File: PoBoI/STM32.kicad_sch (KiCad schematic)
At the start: 24 parts, among them U17 LP5907SNX-3.3, U21 74AC14MTCX, U22 LTC4304CMS#PBF, U26 ISL3259EIRZ, U6 STM32F103RET6, Y1 ABS07-166-32.768KHZ-T

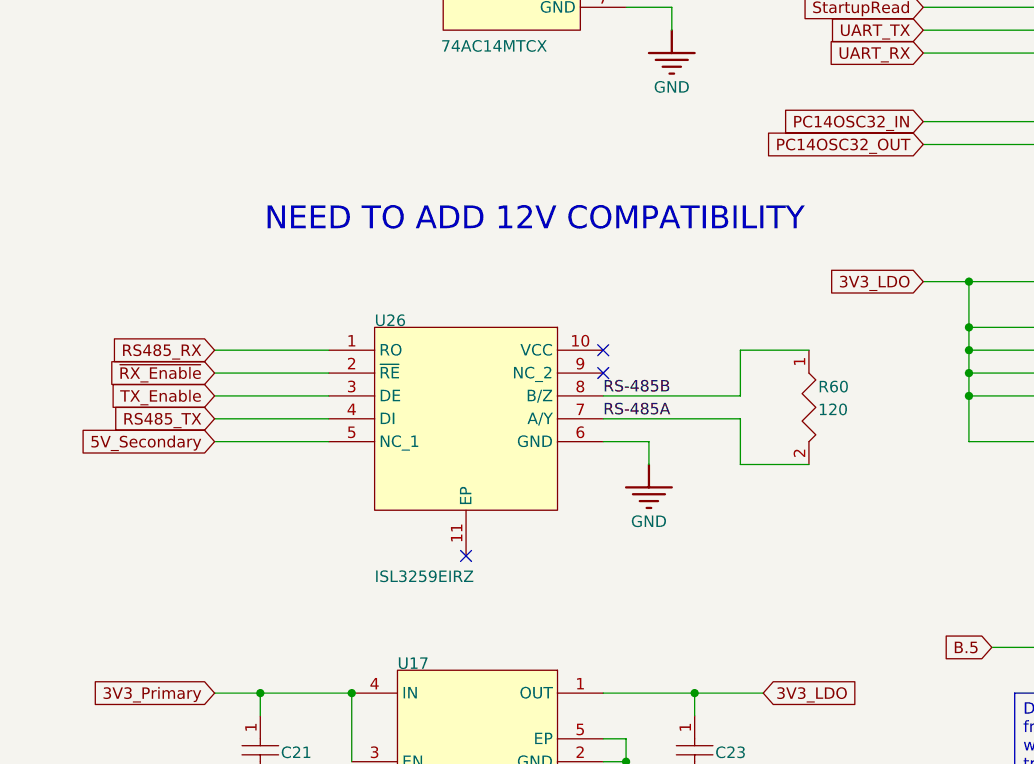
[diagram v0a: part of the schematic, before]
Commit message: POBOI 4S updates: remove 12V/TVS sheets, fix VBATT dividers, INA219 addresses, U26
POBOI changes 10/28 Simon Ionashku

- Deleted the separate copy of the PCB file (BoardFix, it was an older version)
- Removed these sheets from the schematic and the board (no use for them anymore)
   - 12 PRIMARY
   - 12V BOOST
   - 12V SECONDARY
      - our 4S pack is already 12-16.8V so boosting to 12V does nothing, and the LM2622 is only rated for 12V in anyway
      - anything that needs ~12V can just use the VBATT Primary/Secondary rails
      - also deleted the "NEED TO ADD 12V COMPATIBILITY" note on the STM32 sheet
   - TVS_DIODES
      - they weren't actually connected to anything (cathodes were all no-connects)
      - they're also just 3.6V zeners, not real TVS diodes
      - the LTC4231 already shuts off on overvoltage, undervoltage and overcurrent, and there's a small zener clamp on each enable line
- Fixed the VBATT Primary and Secondary divider resistors since they were still using the 2S numbers and we moved to 4S
   - with the old values the switches would've never turned on (they cut off above ~8V)
   - new thresholds: OVoff = 17.5V, UVon = 12.4V, UVoff = 12.0V (3.0V per cell)
   - RES    OLD     NEW
      R71    866k    931k   (Primary)
      R74    2.37k   2.15k  (Primary)
      R77    37.4k   18.7k  (Primary)
      R78    100k    45.3k  (Primary)
      R68    866k    931k   (Secondary)
      R65    2.37k   2.15k  (Secondary)
      R63    37.4k   18.7k  (Secondary)
      R64    100k    45.3k  (Secondary)
   - updated the values, part numbers and form factor (all 0603 now) in the BOM and field table
      - R68/R71 were 0201 rated for 25V which is cutting it close at 16.8V
   - updated the notes and calculations on both sheets
- Fixed the INA219 addresses
   - a bunch of the A0/A1 pins were floating (marked no-connect) so the addresses would've been random
   - went through and checked/corrected all six so A0 and A1 match the slave address table
      5V Primary    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
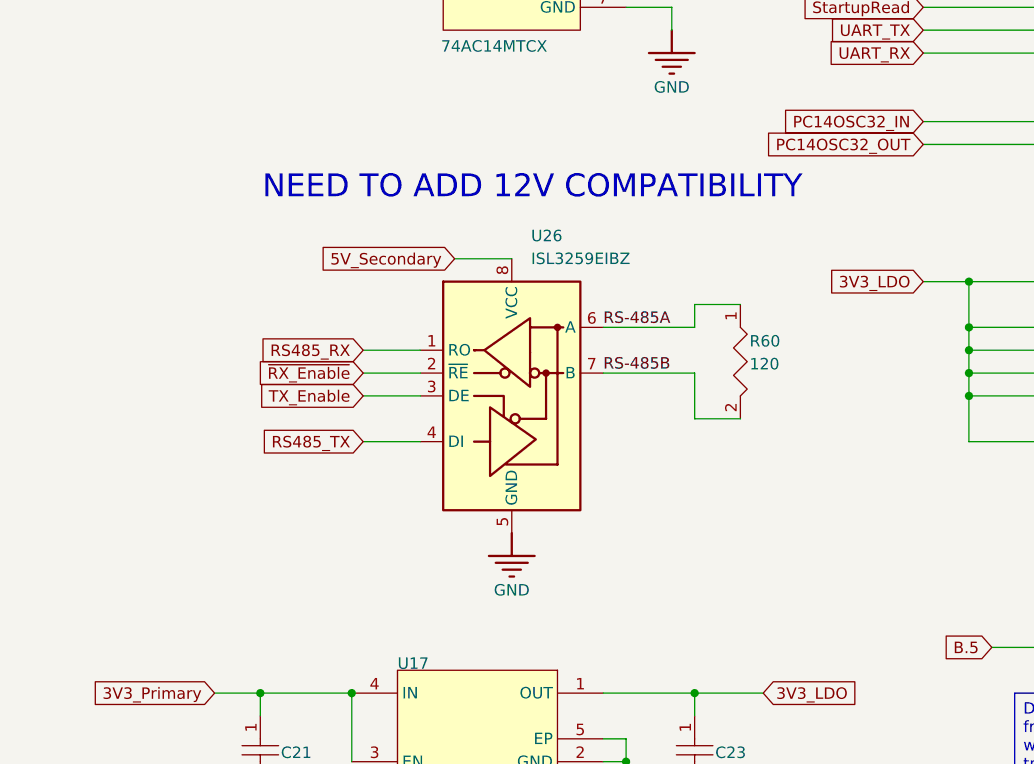
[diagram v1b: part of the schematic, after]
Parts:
- removed U26: ISL3259EIRZ, Vault:ISL3259EIRZ-Footprint-1, symbol UGA SSRL Hardware Team:root_0_ISL3259EIRZ-Symbol-1_UGA SSRL Hardware Team
- added U26: ISL3259EIBZ, Package_SO:SOIC-8_3.9x4.9mm_P1.27mm, symbol Interface_UART:MAX485E
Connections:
- net 5V_Secondary: now also U26.8 (VCC)
- net GND: now also U26.5 (GND)
- net RS-485A: now also R60.1, U26.6 (A); no longer R60.2
- net RS-485B: now also R60.2, U26.7 (B); no longer R60.1
- net RS485_RX: now also U26.1 (RO)
- net RS485_TX: now also U26.4 (DI)
- net TX_Enable: now also U26.3 (DE)
- net ~{RX_Enable}: now also U26.2 (~{RE})
- no-connect marks 12 -> 9
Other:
- moved on the sheet: R60
